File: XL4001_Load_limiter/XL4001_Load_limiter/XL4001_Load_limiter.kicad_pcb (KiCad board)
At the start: 2 copper layers, 90 x 85 mm, 79 parts, among them J1 5.08-2P-90, J3 Conn_01x03_Socket, J4 1Wire, K1 G5LE-1, K2 G5LE-1, Q1 2N7002K, Q2 PMOS, Q3 2N7002K, Q5 2N7002K, Q6 2N7002K, Q7 40N02, U2 XL1509-5.0, U3 AP2112K-3.3, U4 HDC1080, U5 ESP32-C3-Supermini, U6 XL1509-12E1, U7 PC817XI

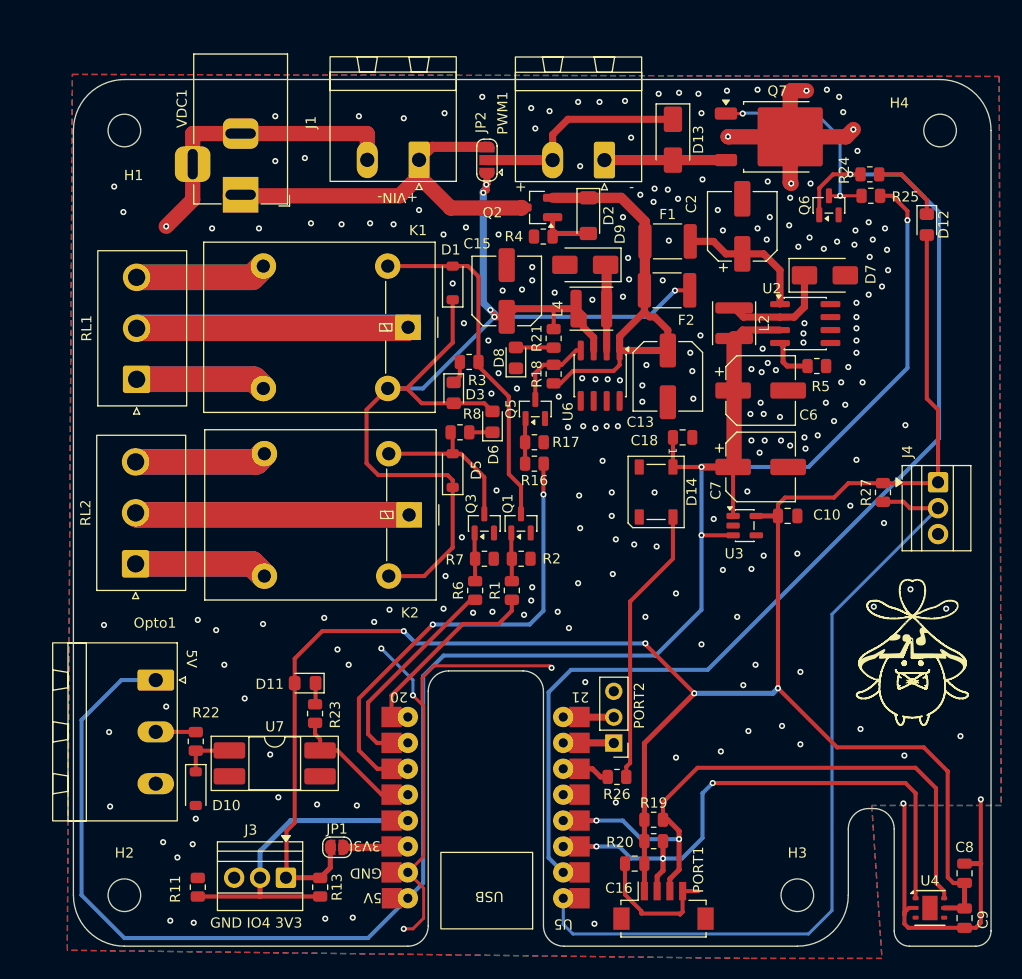
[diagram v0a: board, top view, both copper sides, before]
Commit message: Added base layout for Load Limiter
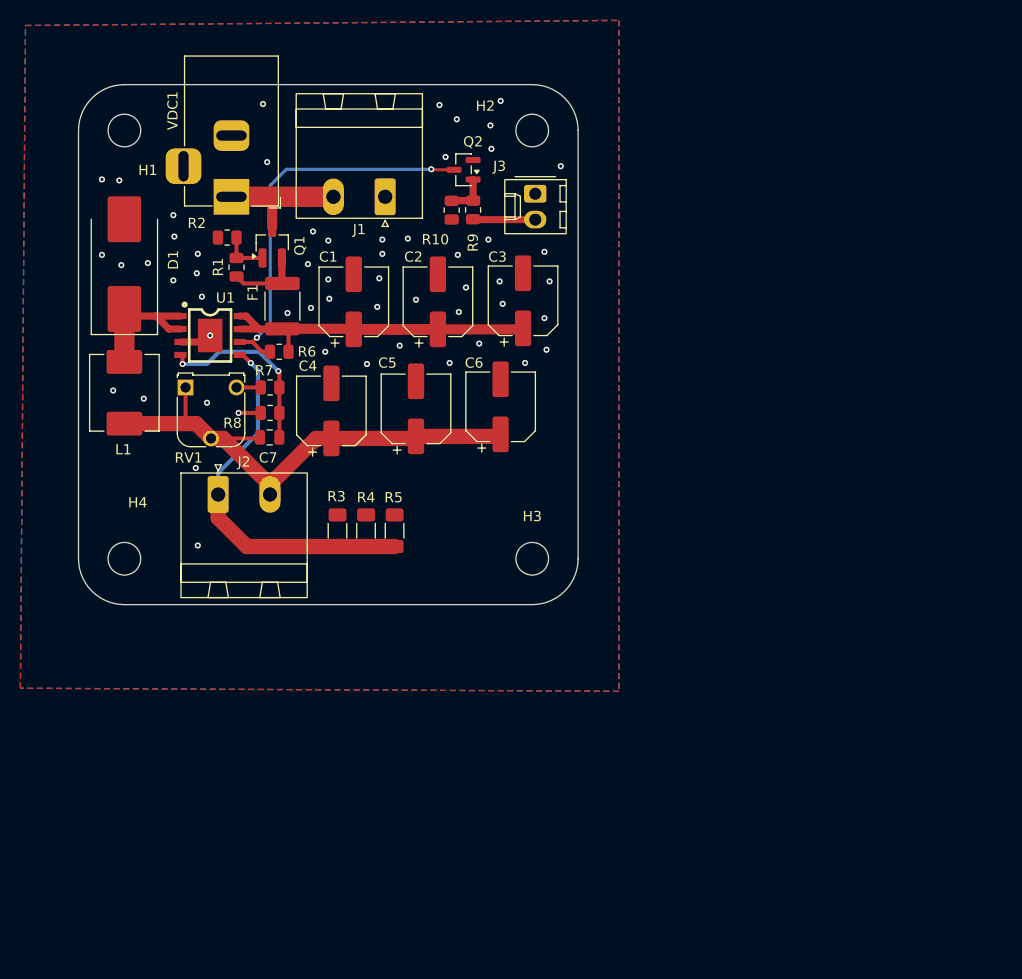
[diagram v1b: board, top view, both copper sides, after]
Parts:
- removed C10, C16, C8: 10u, Capacitor_SMD:C_0805_2012Metric
- removed C13, C15: 100uF, Capacitor_SMD:C_Elec_6.3x7.7
- removed C18, C9: 100nF, Capacitor_SMD:C_0805_2012Metric
- removed D10, D5: 1N4148W, Diode_SMD:D_SOD-123
- removed D11, D12, D8: LED, LED_SMD:LED_0805_2012Metric_Pad1.15x1.40mm_HandSolder
- removed D13, D7, D9: SS14, Diode_SMD:D_SMA
- removed D14: WS2812B, LED_SMD:LED_WS2812B_PLCC4_5.0x5.0mm_P3.2mm
- removed D2: D_Zener, Diode_SMD:D_MiniMELF
- removed D3, D6: LED_RED, LED_SMD:LED_0805_2012Metric_Pad1.15x1.40mm_HandSolder
- removed F2: Bypass fuse, Fuse:Fuse_1812_4532Metric_Pad1.30x3.40mm_HandSolder
- removed J4: 1Wire, TerminalBlock:TerminalBlock_Xinya_XY308-2.54-3P_1x03_P2.54mm_Horizontal
- removed JP1: SolderJumper_2_Open, Jumper:SolderJumper-2_P1.3mm_Open_RoundedPad1.0x1.5mm
- removed JP2: SolderJumper_3_Open, Jumper:SolderJumper-3_P1.3mm_Open_RoundedPad1.0x1.5mm
- removed K1, K2: G5LE-1, Relay_THT:Relay_SPDT_Omron-G5LE-1
- removed L2, L4: 33u, Inductor_SMD:L_Sunlord_SWPA4010S
- removed Opto1: Conn_01x03_Pin, Connector_Phoenix_MSTB:PhoenixContact_MSTBA_2,5_3-G-5,08_1x03_P5.08mm_Horizontal
- removed PORT1: Conn_01x04_Socket, Connector_Hirose:Hirose_DF13C_CL535-0404-8-51_1x04-1MP_P1.25mm_Vertical
- removed PORT2: Conn_01x03_Socket, Connector_PinHeader_2.54mm:PinHeader_1x03_P2.54mm_Vertical
- removed PWM1: 5.08-2P-90, Connector_Phoenix_MSTB:PhoenixContact_MSTBA_2,5_2-G-5,08_1x02_P5.08mm_Horizontal
- removed Q3, Q5, Q6: 2N7002K, Package_TO_SOT_SMD:SOT-23
- removed Q7: 40N02, Package_TO_SOT_SMD:TO-252-2
- removed R11, R13, R17, R18, R21, R22, R27: 10k, Resistor_SMD:R_0805_2012Metric
- removed R16, R26: 330, Resistor_SMD:R_0805_2012Metric
- removed R19, R20, R25: 2k2, Resistor_SMD:R_0805_2012Metric
- removed R23, R24: 1k, Resistor_SMD:R_0805_2012Metric
- removed RL1, RL2: Conn_01x03_Socket, Connector_JST:JST_NV_B03P-NV_1x03_P5.00mm_Vertical
- removed U2: XL1509-5.0, Package_SO:SOIC-8_3.9x4.9mm_P1.27mm
- removed U3: AP2112K-3.3, Package_TO_SOT_SMD:SOT-23-5
- removed U4: HDC1080, Package_SON:Texas_PWSON-N6
- removed U5: ESP32-C3-Supermini, Custom_Footprints:ESP32-C3-Supermini
- removed U6: XL1509-12E1, Package_SO:SOIC-8_3.9x4.9mm_P1.27mm
- removed U7: PC817XI, Package_DIP:DIP-4_W8.89mm_SMDSocket_LongPads
- added C1: 220uF, Capacitor_SMD:CP_Elec_6.3x7.7, F.Cu at (144.8, 77.6)
- added C3: 220uF, Capacitor_SMD:CP_Elec_6.3x7.7, F.Cu at (161.4, 77.5)
- added C4: 220uF, Capacitor_SMD:CP_Elec_6.3x7.7, F.Cu at (142.6, 88.3)
- added C5: 220uF, Capacitor_SMD:CP_Elec_6.3x7.7, F.Cu at (150.9, 88.1)
- added J2: 5.08-2P-90, Connector_Phoenix_MSTB:PhoenixContact_MSTBA_2,5_2-G-5,08_1x02_P5.08mm_Horizontal, F.Cu at (131.5, 96.5)
- added L1: 33u, Inductor_SMD:L_Chilisin_BMRx00060630, F.Cu at (122.3, 86.5)
- added R10: 10k, Resistor_SMD:R_0805_2012Metric, F.Cu at (154.4, 68.6)
- added R9: 1k, Resistor_SMD:R_0805_2012Metric, F.Cu at (156.5, 68.6)
- added RV1: 10k, Potentiometer_THT:Potentiometer_Runtron_RM-065_Vertical, F.Cu at (128.3, 86.0)
- added U1: XL4001, Aleoexpress:ESOP-8_L4.9-W3.9-P1.27-LS6.0-BL-EP, F.Cu at (130.7, 80.9)
- C7: value 220uF -> 33nF; footprint Capacitor_SMD:CP_Elec_6.3x7.7 -> Capacitor_SMD:C_0805_2012Metric
- D1: value 1N4148W -> SS34; footprint Diode_SMD:D_SOD-123 -> Diode_SMD:D_SMC_Handsoldering
- F1: value 1.1A Polyfuse -> Polyfuse; footprint Fuse:Fuse_1812_4532Metric_Pad1.30x3.40mm_HandSolder -> Resistor_SMD:R_1812_4532Metric_Pad1.30x3.40mm_HandSolder
- J3: value Conn_01x03_Socket -> Conn_01x02_Socket; footprint TerminalBlock:TerminalBlock_Xinya_XY308-2.54-3P_1x03_P2.54mm_Horizontal -> Connector_Molex:Molex_KK-254_AE-6410-02A_1x02_P2.54mm_Vertical
- Q1: value 2N7002K -> PMOS; footprint Package_TO_SOT_SMD:SOT-23 -> Package_TO_SOT_SMD:SOT-23_Handsoldering
- Q2: value PMOS -> 2N7002K; footprint Package_TO_SOT_SMD:SOT-23_Handsoldering -> Package_TO_SOT_SMD:SOT-23
- R1, R6: value 330 -> 10k
- R3: value 2.2k -> 250mR 1W 1%; footprint Resistor_SMD:R_0805_2012Metric -> Resistor_SMD:R_1206_3216Metric_Pad1.30x1.75mm_HandSolder
- R4: value 10k -> 250mR 1W 1%; footprint Resistor_SMD:R_0805_2012Metric -> Resistor_SMD:R_1206_3216Metric_Pad1.30x1.75mm_HandSolder
- R5: value 100k -> 250mR 1W 1%; footprint Resistor_SMD:R_0805_2012Metric -> Resistor_SMD:R_1206_3216Metric_Pad1.30x1.75mm_HandSolder
- R7: value 10k -> 8.2k
- R8: value 2.2k -> 1k
- moved H4 90.4 mm to (122.3, 102.8)
- moved H2 85.0 mm to (162.3, 60.8)
- moved J3 71.4 mm to (162.6, 67.0), turned to -90 degrees
- moved C7 48.2 mm to (136.6, 90.9), turned to 180 degrees
- moved R5 44.5 mm to (148.8, 100.0), turned to 90 degrees
- moved R2 42.7 mm to (132.4, 71.3), turned to 180 degrees
- moved H3 42.0 mm to (162.3, 102.8)
- moved R1 41.6 mm to (133.3, 74.2)
- moved F1 38.3 mm to (137.8, 78.0), turned to -90 degrees
- moved Q1 36.8 mm to (136.8, 71.8)
- moved R4 33.7 mm to (146.0, 100.0), turned to 90 degrees
- moved D1 32.3 mm to (122.3, 73.9)
- moved C2 30.8 mm to (153.1, 77.6)
- moved R6 30.3 mm to (137.5, 82.5), turned to 0 degrees
- moved R7 26.9 mm to (136.6, 86.0)
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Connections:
- C2 pad 1: Net-(U2-VIN) -> VCC
- C6 pad 1: +5V -> PCH0
- C7 pad 1: +5V -> FB_CH0
- C7 pad 2: GND -> PCH0
- D1 pad 1: relayPWR -> Net-(D1-K)
- D1 pad 2: Net-(D1-A) -> GND
- F1 pad 1: VCC -> Net-(Q1-S)
- F1 pad 2: Net-(U2-VIN) -> VCC
- J1 pad 1: Vin -> GND
- J1 pad 2: GND -> Vin
- J3 pad 1: +3.3V -> GND
- J3 pad 2: ADC -> Net-(J3-Pin_2)
- Q1 pad 2: GND -> Net-(Q1-S)
- Q1 pad 3: Net-(D1-A) -> Vin
- Q2 pad 1: Net-(D2-A) -> CH0
- Q2 pad 2: VCC -> GND
- Q2 pad 3: Vin -> EN_CH0
- R1 pad 1: RELAY0_PIN -> Net-(Q1-S)
- R3 pad 1: Net-(D1-A) -> NCH0
- R3 pad 2: Net-(D3-K) -> GND
- R4 pad 1: Net-(D2-A) -> NCH0
- R5 pad 1: PWR_EN -> NCH0
- R6 pad 1: RELAY1_PIN -> EN_CH0
- R6 pad 2: Net-(Q3-G) -> VCC
- R7 pad 1: Net-(Q3-G) -> Net-(R7-Pad1)
- R7 pad 2: GND -> FB_CH0
- R8 pad 1: Net-(D5-A) -> FB_CH0
- R8 pad 2: Net-(D6-K) -> GND
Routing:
- net +5V: track 210.1 -> 0.00 mm, vias 3 -> 0
- net +3.3V: track 199.6 -> 0.00 mm, vias 4 -> 0
- net GND: track 149.4 -> 5.35 mm, vias 222 -> 56
- net relayPWR: track 119.4 -> 0.00 mm, vias 5 -> 0
- net openDrain: track 106.5 -> 0.00 mm, vias 1 -> 0
- net 1Wire: track 79.7 -> 0.00 mm
- net SCL: track 65.5 -> 0.00 mm, vias 2 -> 0
- net SDA: track 59.9 -> 0.00 mm, vias 3 -> 0
- net Net-(RL2-Pin_2): track 53.8 -> 0.00 mm
- net Net-(RL1-Pin_2): track 53.3 -> 0.00 mm
- net PCH0: track 0.00 -> 53.0 mm
- net 12V_enable: track 45.1 -> 0.00 mm, vias 2 -> 0
- net EN_CH0: track 0.00 -> 38.2 mm, vias 0 -> 2
- net NCH0: track 0.00 -> 37.0 mm, vias 0 -> 1
- net Net-(D1-A): track 34.3 -> 0.00 mm
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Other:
- board size 90 x 85 mm -> 49 x 51 mm
- board text removed: "+"
- board text removed: "+VIN-"
- board text removed: "-"
- board text removed: "5V"
- board text removed: "GND IO4 3V3"

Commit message: Hotfixes
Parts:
- added D16: LED_GREEN, LED_SMD:LED_0805_2012Metric_Pad1.15x1.40mm_HandSolder, F.Cu at (155.4, 94.3)
- added R11: 8.2k, Resistor_SMD:R_0805_2012Metric, F.Cu at (155.4, 98.3)
- D1: footprint Diode_SMD:D_SMC_Handsoldering -> Diode_SMD:D_SMA
- moved D1 2.60 mm to (122.3, 76.5)
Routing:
- net EN_CH0: track 38.2 -> 34.3 mm, vias 2 -> 4
- net PCH0: track 53.0 -> 55.5 mm
- net Net-(D16-K): track 0.00 -> 2.05 mm
- net FB_CH0: track 18.2 -> 17.5 mm
- net GND: vias 56 -> 76
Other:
- board text added: "- +"
- board text added: "12<Vout<26"
- board text added: "I(lim)=0.15/R"
- board text added: "INPUT"
- board text added: "OUTPUT"
